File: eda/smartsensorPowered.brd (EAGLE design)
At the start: 47 x 26.7 mm, 38 parts, among them Q1 IRFML8244, Q2 IRFML8244, Q3 IRFML8244, Q4 IRFML8244, U1 ISL83491SOIC, U2 ATTINY1634

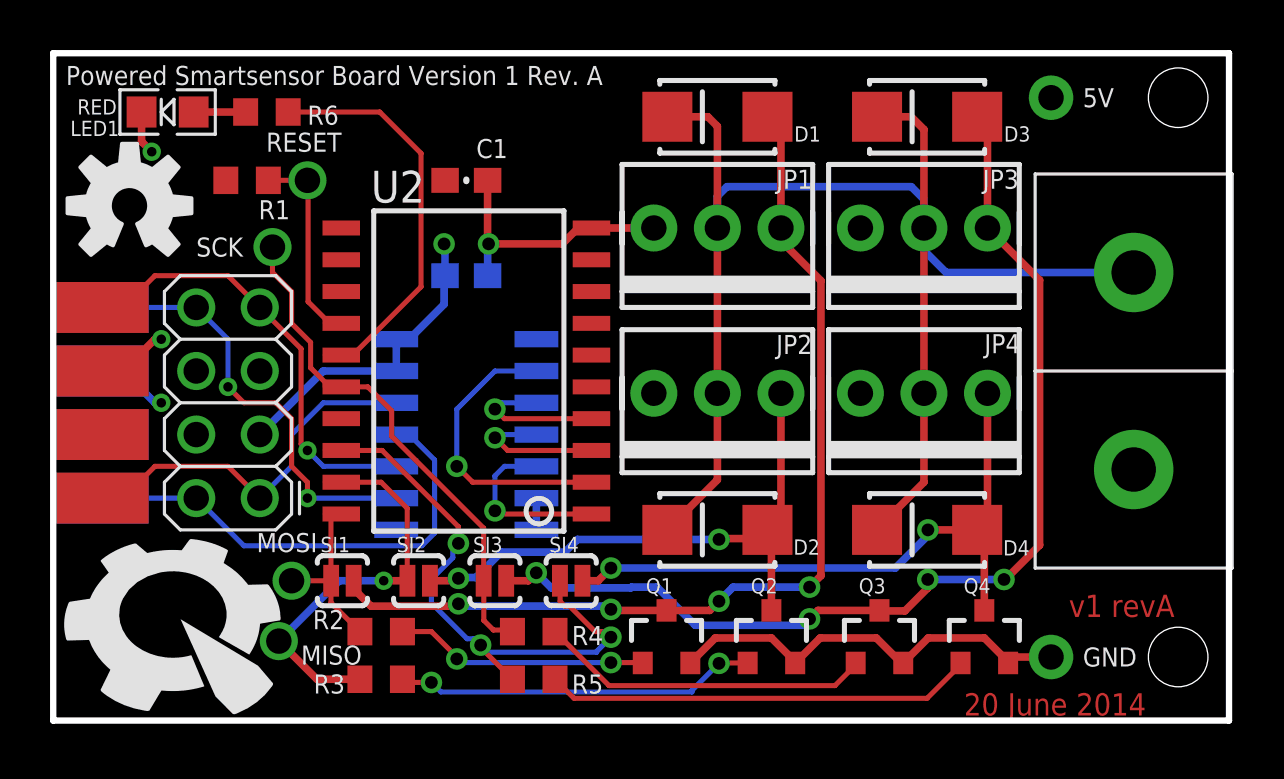
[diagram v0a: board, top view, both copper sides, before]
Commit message: Replaced 2x4 connectors with 2x5's.
On smartsensor, smartsensorPowered, smartsensor_powered_jig, and team_flag.
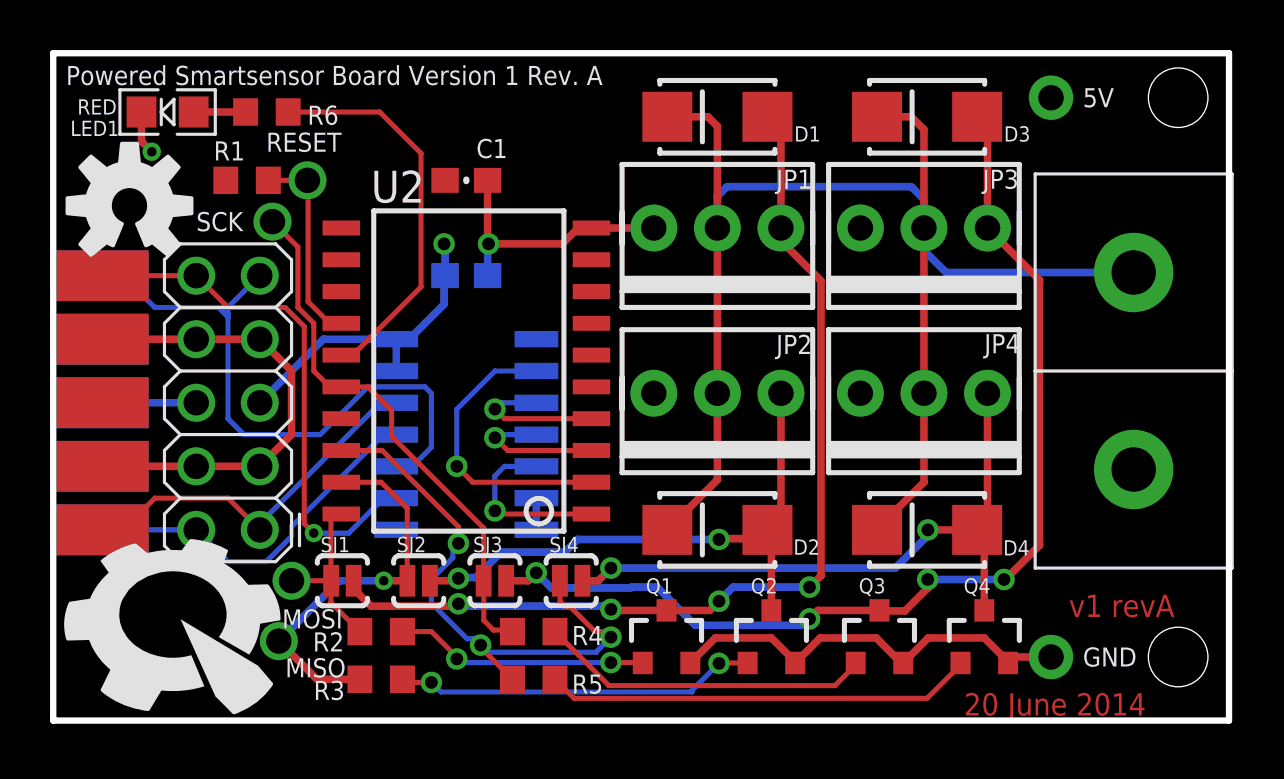
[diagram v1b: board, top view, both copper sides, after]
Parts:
- U$12: value SENSOR_CONPTH -> SENSOR_CON_5PINPTH; device pie:2X4 -> pie:2X5
- U$13: value SENSOR_CONSMD-EDGE -> SENSOR_CON_5PINSMD-EDGE; device pie:2X4-EDGE -> pie:2X5-EDGE
- moved SCK 1.02 mm to (8.76, 19.9)
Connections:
- net 5V: now also U$12.5, U$13.5; no longer U$12.3, U$13.3
- net B_N: now also U$12.9, U$13.9; no longer U$12.7, U$13.7
- net B_P: now also U$12.10, U$13.10; no longer U$12.8, U$13.8
- net GND: now also U$12.3, U$12.7, U$12.8, U$13.3, U$13.7, U$13.8; no longer U$12.5, U$13.5
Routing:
- net GND: track 34.1 -> 49.9 mm, vias 3 -> 2
- net B_N: track 17.7 -> 25.8 mm, vias 1 -> 0
- net A_N: track 19.2 -> 14.7 mm
- net B_P: track 17.6 -> 21.3 mm, vias 2 -> 1
- net 5V: track 16.2 -> 17.6 mm, vias 2 -> 1
- net IO3: track 20.9 -> 21.9 mm
